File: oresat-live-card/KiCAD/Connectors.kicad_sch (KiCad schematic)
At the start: 14 parts, among them J1 ORESAT-DEBUG-CONNECTOR-CARD, J4 TFM-120-01-L-D-RA, J6 J-MOLEX-SMPM-73300-003X

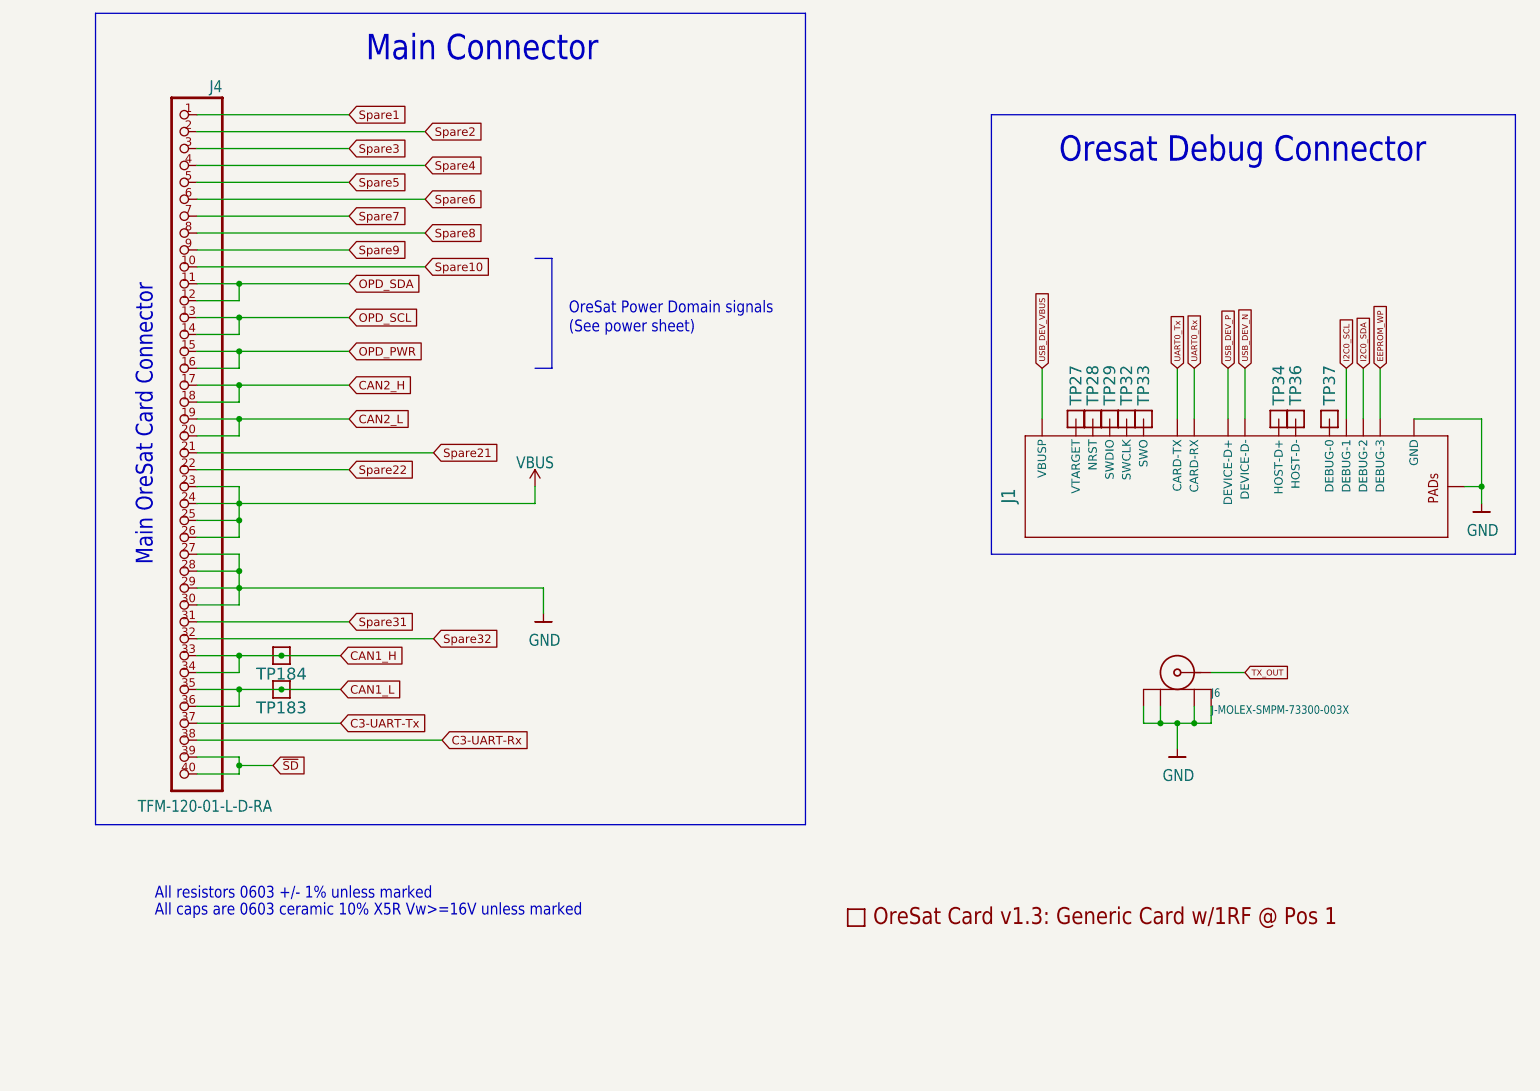
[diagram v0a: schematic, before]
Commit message: Updated OreSat Live Card. Added changes from the C3 v6 Octavo circuitry and GPS card update. Fixed some GitHub issues. Board layout still in progress.
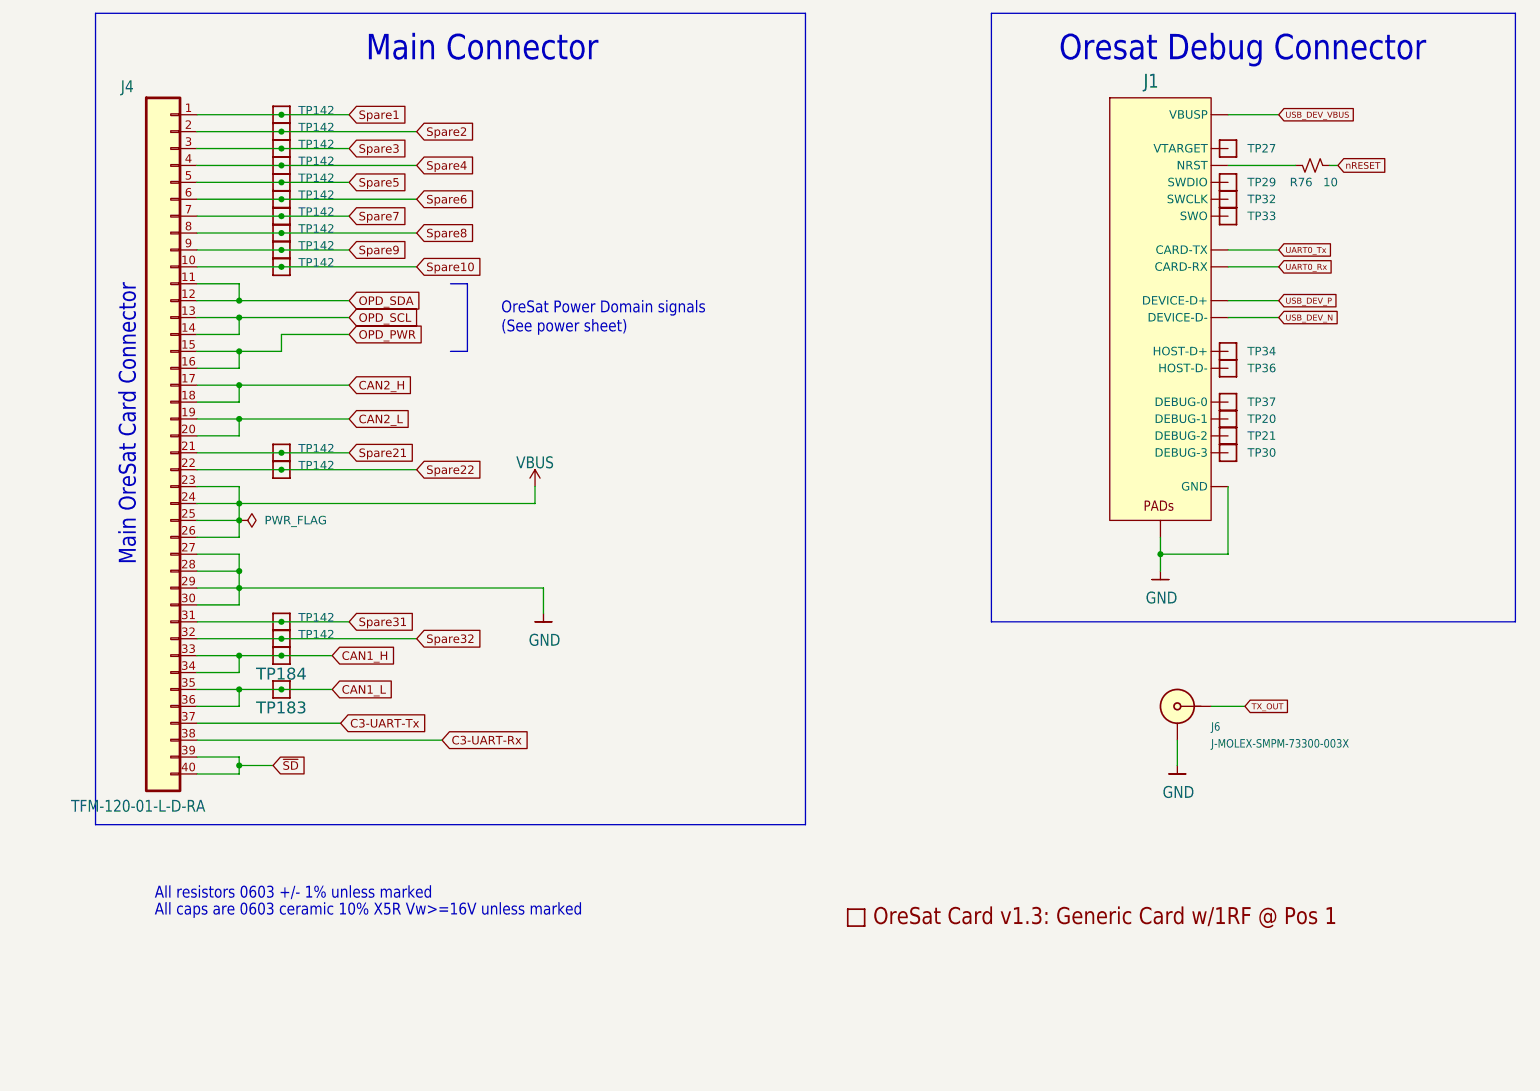
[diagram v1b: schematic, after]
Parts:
- removed TP28: TEST-POINT, oresat-live-card:PAD.03X.04, symbol oresat-live-card-eagle-import:TEST-POINT
- added R76: 10, Resistor_SMD:R_0603_1608Metric, symbol Device:R_Small_US
- added TP142 (x14): 0.03x0.04, oresat-misc:TestPoint_Pad_D1.0mm, symbol oresat-misc:Test-Point-1mm-round
- added TP20, TP21, TP30: TEST-POINT, oresat-misc:TestPoint_Pad_D1.0mm, symbol oresat-misc:Test-Point-1mm-round
- J1: footprint oresat-live-card:TE_2-1734592-0 -> oresat-connectors:J-TE-2-1734592-0; symbol oresat-live-card-eagle-import:ORESAT-DEBUG-CONNECTOR-CARD -> oresat-connectors:J-TE-2-1734592-0
- J4: footprint oresat-live-card:J-SAMTEC-TFM-120-X1-XXX-D-RA -> oresat-connectors:J-SAMTEC-TFM-120-X1-XXX-D-RA; symbol oresat-live-card-eagle-import:J-SAMTEC-TFM-120-X1-XXX-D-RA -> oresat-connectors:J-SAMTEC-TFM-120-01-L-D-RA
- J6: footprint oresat-footprints:J-MOLEX-SMPM-073300-003X -> oresat-connectors:J-MOLEX-SMPM-073300-002X; symbol oresat-live-card-eagle-import:J-MOLEX-SMPM-73300-003X -> oresat-connectors:J-MOLEX-SMPM-73300-002X
- TP183, TP184, TP27, TP29, TP32, TP33, TP34, TP36, TP37: footprint oresat-live-card:PAD.03X.04 -> oresat-misc:TestPoint_Pad_D1.0mm; symbol oresat-live-card-eagle-import:TEST-POINT -> oresat-misc:Test-Point-1mm-round
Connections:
- net GND: now also J6.SHLD; no longer J6.GND (SHIELD3)
- net Spare1: now also TP142.1
- net Spare10: now also TP142.1
- net Spare2: now also TP142.1
- net Spare21: now also TP142.1
- net Spare22: now also TP142.1
- net Spare3: now also TP142.1
- net Spare31: now also TP142.1
- net Spare32: now also TP142.1
- net Spare4: now also TP142.1
- net Spare5: now also TP142.1
- net Spare6: now also TP142.1
- net Spare7: now also TP142.1
- net Spare8: now also TP142.1
- net Spare9: now also TP142.1
- net TX_OUT: now also J6.SIG; no longer J6.RF (CENTER)
- net at J1.10 (NRST): now also R76.1
- net EEPROM_WP: no longer names the net of J1.20 (DEBUG-3)
- net EEPROM_WP: now also TP30.1
- net I2C0_SCL: no longer names the net of J1.18 (DEBUG-1)
- net I2C0_SCL: now also TP20.1
- net I2C0_SDA: no longer names the net of J1.19 (DEBUG-2)
- net I2C0_SDA: now also TP21.1
- new net nRESET: R76.2
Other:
- moved on the sheet: TP27, TP29, TP32, TP33, TP34, TP36, TP37

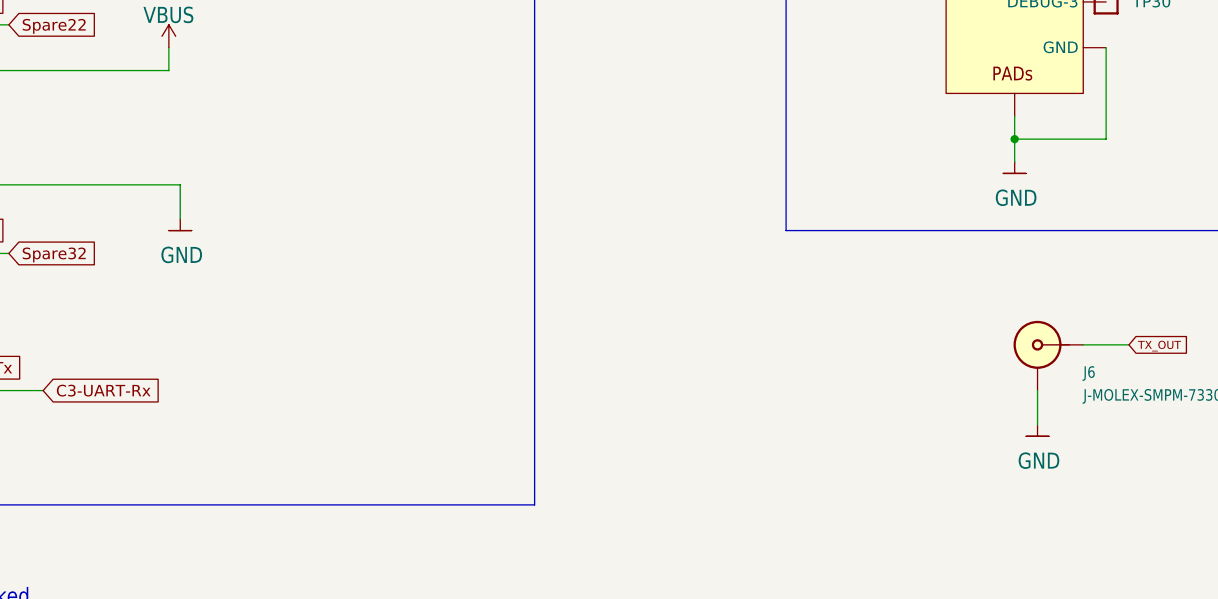
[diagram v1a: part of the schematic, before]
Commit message: Cleaned up ERC and DRC errors on DxWiFi Card
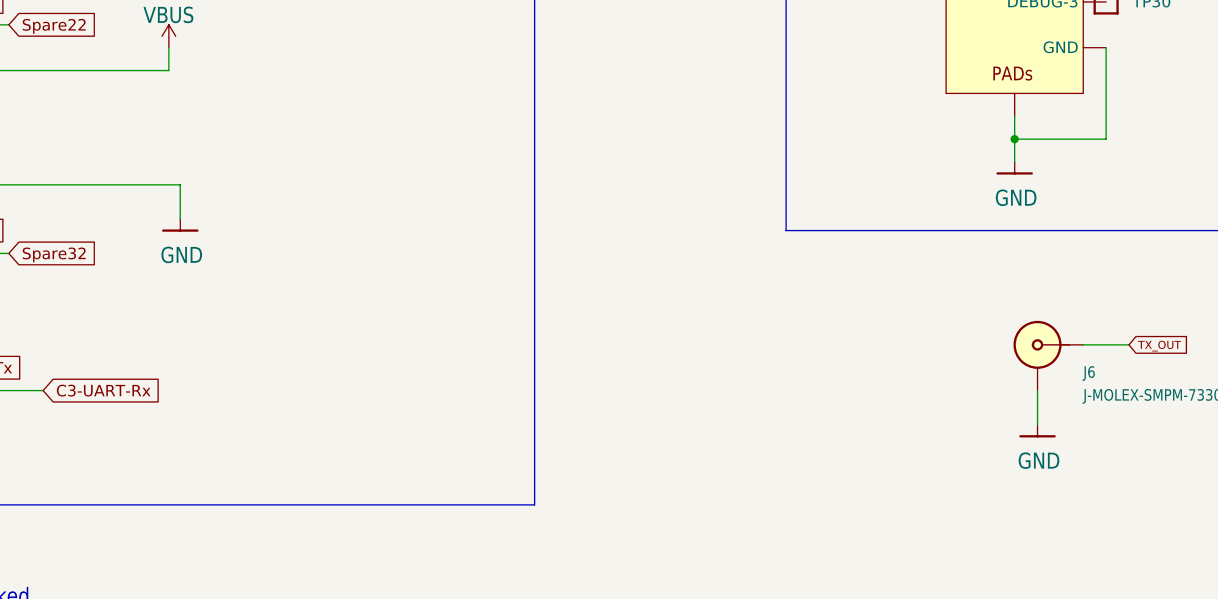
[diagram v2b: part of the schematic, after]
